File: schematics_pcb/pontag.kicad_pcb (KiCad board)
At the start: 2 copper layers, 35 parts, among them J1 12V Selector, J2 External 12V, J3 RS232 Port, J4 PS/2 Mouse, J5 AVR-ISP-6, J6 External 5V, J7 Extra, SW1 Reset, U1 L78L05_TO92, U3 ATmega328P-PU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

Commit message: Draw the circuit for pontag
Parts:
- C5, C6: moved to B.Cu
- moved C4 69.3 mm to (185.4, 99.1), turned to 180 degrees
- moved C5 69.1 mm to (201.9, 82.5), turned to 180 degrees
- moved D5 68.7 mm to (182.9, 111.8), turned to 180 degrees
- moved J6 60.6 mm to (179.1, 99.1)
- moved JP1 56.9 mm to (182.9, 106.7), turned to 270 degrees
- moved JP2 55.0 mm to (201.9, 92.7)
- moved C6 49.9 mm to (193.0, 119.4), turned to 90 degrees
- moved J5 46.2 mm to (205.7, 106.7)
- moved R2 42.4 mm to (185.4, 116.8), turned to 180 degrees
- moved R4 42.3 mm to (208.3, 143.5), turned to 180 degrees
- moved U3 24.7 mm to (196.8, 134.6)
- moved J7 24.7 mm to (182.9, 121.9)
- moved J4 24.3 mm to (191.8, 143.5)
- moved U1 24.0 mm to (196.8, 91.4), turned to 180 degrees
- moved R1 21.6 mm to (200.7, 121.9)
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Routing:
- net GND: track 0.00 -> 264.5 mm, vias 0 -> 1
- net VCC: track 0.00 -> 170.9 mm
- net /TTL-RX: track 0.00 -> 49.9 mm, vias 0 -> 1
- net /RESET: track 0.00 -> 47.7 mm
- net /TTL-TX: track 0.00 -> 46.6 mm, vias 0 -> 1
- net /TTL-CTS: track 0.00 -> 40.2 mm, vias 0 -> 1
- net /SCK: track 0.00 -> 39.3 mm
- net /PS2-DATA: track 0.00 -> 35.2 mm
- net /RS232-RTS: track 0.00 -> 35.0 mm, vias 0 -> 1
- net /RS232-TX: track 0.00 -> 34.5 mm, vias 0 -> 1
- net /PS2-CLOCK: track 0.00 -> 32.3 mm, vias 0 -> 1
- net +12V: track 0.00 -> 23.1 mm
- net /MISO: track 0.00 -> 21.7 mm, vias 0 -> 1
- net Net-(C4-Pad1): track 0.00 -> 21.5 mm
- net /RS232-DTR: track 0.00 -> 20.9 mm
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- added copper zone on B.Cu, net GND
- added copper zone on F.Cu, net GND
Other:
- board outline added: 38.1 x 85.1 mm

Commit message: Add silkscreen
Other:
- board text added: "PS/2 -> RS232 (Microsoft protocol) mouse adapter"
- board text added: "Pontag - Proto 00"
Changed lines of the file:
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@@
   (general
     (thickness 1.6)
-    (drawings 4)
+    (drawings 6)
     (tracks 290)
     (zones 0)
@@
     )
   )
+  (gr_text "PS/2 -> RS232 (Microsoft protocol) mouse adapter" (at 177.8 128.27 270) (layer B.SilkS)
+    (effects (font (size 1 1) (thickness 0.15)) (justify mirror))
+  )
+  (gr_text "Pontag - Proto 00" (at 210.82 134.62 -90) (layer B.SilkS)
+    (effects (font (size 2 2) (thickness 0.15)) (justify mirror))
+  )
   (gr_line (start 175.26 149.86) (end 175.26 64.77) (layer Edge.Cuts) (width 0.1))

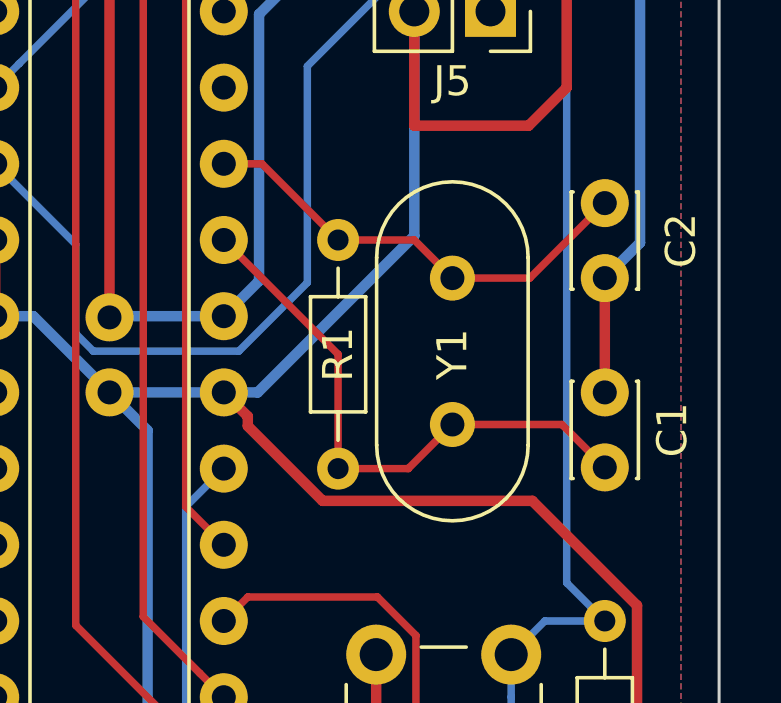
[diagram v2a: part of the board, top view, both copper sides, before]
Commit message: Fix DRC error
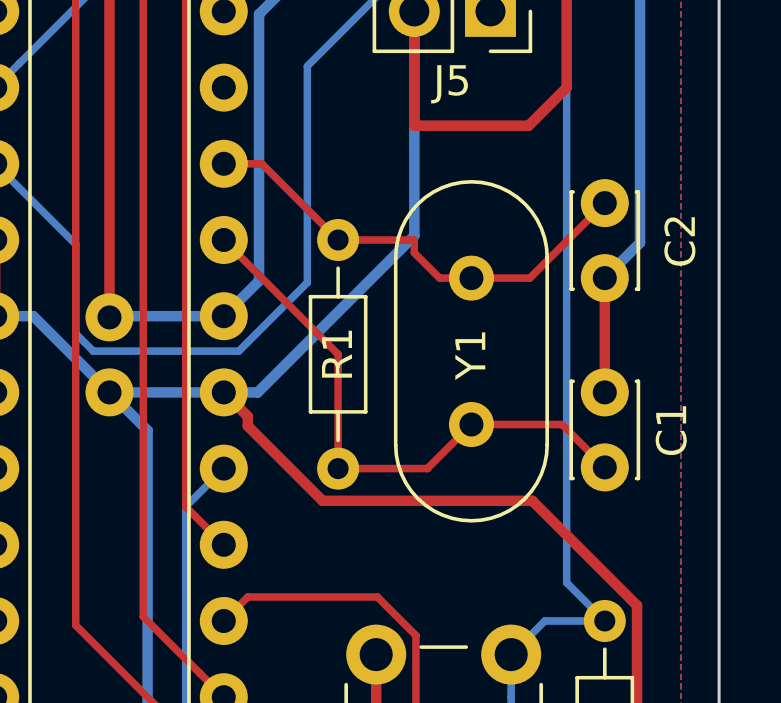
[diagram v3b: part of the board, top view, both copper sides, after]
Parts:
- moved Y1 0.63 mm to (205.1, 115.6)
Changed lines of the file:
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@@
     (thickness 1.6)
     (drawings 6)
-    (tracks 290)
+    (tracks 292)
     (zones 0)
     (modules 35)
@@
   (page A4)
   (layers
-    (0 F.Cu signal hide)
-    (31 B.Cu signal hide)
+    (0 F.Cu signal)
+    (31 B.Cu signal)
     (32 B.Adhes user)
     (33 F.Adhes user)
@@
   )
   (module Crystal:Crystal_HC49-U_Vertical (layer F.Cu)
-    (at 204.47 115.57 270)
+    (at 205.105 115.57 270)
     (descr "Crystal THT HC-49/U http://5hertz.com/pdfs/04404_D.pdf")
     (tags "THT crystalHC-49/U")
@@
   (gr_line (start 213.36 64.77) (end 213.36 149.86) (layer Edge.Cuts) (width 0.1))
   (gr_line (start 175.26 64.77) (end 213.36 64.77) (layer Edge.Cuts) (width 0.1))
+  (segment (start 208.12 120.45) (end 209.55 121.88) (width 0.25) (layer F.Cu) (net 1))
   (segment (start 200.66 118.11) (end 196.85 114.3) (width 0.25) (layer F.Cu) (net 1))
   (segment (start 200.66 121.92) (end 200.66 118.11) (width 0.25) (layer F.Cu) (net 1))
-  (segment (start 203 121.92) (end 204.47 120.45) (width 0.25) (layer F.Cu) (net 1))
-  (segment (start 200.66 121.92) (end 203 121.92) (width 0.25) (layer F.Cu) (net 1))
-  (segment (start 208.12 120.45) (end 209.55 121.88) (width 0.25) (layer F.Cu) (net 1))
-  (segment (start 204.47 120.45) (end 208.12 120.45) (width 0.25) (layer F.Cu) (net 1))
+  (segment (start 203.635 121.92) (end 205.105 120.45) (width 0.25) (layer F.Cu) (net 1))
+  (segment (start 200.66 121.92) (end 203.635 121.92) (width 0.25) (layer F.Cu) (net 1))
+  (segment (start 205.105 120.45) (end 208.12 120.45) (width 0.25) (layer F.Cu) (net 1))
   (segment (start 199.85 69.4) (end 199.85 67.31) (width 0.35) (layer F.Cu) (net 2))
   (segment (start 195.59 73.66) (end 199.85 69.4) (width 0.35) (layer F.Cu) (net 2))
@@
   (segment (start 197.32 146.36) (end 197.32 139.23) (width 0.35) (layer F.Cu) (net 2))
   (segment (start 201.93 134.62) (end 201.93 128.12) (width 0.35) (layer F.Cu) (net 2))
+  (segment (start 196.85 111.76) (end 198.12 111.76) (width 0.25) (layer F.Cu) (net 3))
+  (segment (start 207.05 115.57) (end 209.55 113.07) (width 0.25) (layer F.Cu) (net 3))
+  (segment (start 200.66 114.3) (end 203.2 114.3) (width 0.25) (layer F.Cu) (net 3))
   (segment (start 198.12 111.76) (end 200.66 114.3) (width 0.25) (layer F.Cu) (net 3))
-  (segment (start 196.85 111.76) (end 198.12 111.76) (width 0.25) (layer F.Cu) (net 3))
-  (segment (start 203.2 114.3) (end 204.47 115.57) (width 0.25) (layer F.Cu) (net 3))
-  (segment (start 200.66 114.3) (end 203.2 114.3) (width 0.25) (layer F.Cu) (net 3))
-  (segment (start 207.05 115.57) (end 209.55 113.07) (width 0.25) (layer F.Cu) (net 3))
-  (segment (start 204.47 115.57) (end 207.05 115.57) (width 0.25) (layer F.Cu) (net 3))
+  (segment (start 207.05 115.57) (end 205.105 115.57) (width 0.25) (layer F.Cu) (net 3))
+  (segment (start 204.04434 115.57) (end 203.2 114.72566) (width 0.25) (layer F.Cu) (net 3))
+  (segment (start 205.105 115.57) (end 204.04434 115.57) (width 0.25) (layer F.Cu) (net 3))
+  (segment (start 203.2 114.72566) (end 203.2 114.3) (width 0.25) (layer F.Cu) (net 3))
   (segment (start 181.61 87.63) (end 179.07 87.63) (width 0.35) (layer F.Cu) (net 4))
   (segment (start 179.19 92.71) (end 180.34 92.71) (width 0.35) (layer F.Cu) (net 4))
